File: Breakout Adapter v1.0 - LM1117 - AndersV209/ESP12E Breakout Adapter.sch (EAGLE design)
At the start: 11 parts, among them IC1 LM1117-3.3

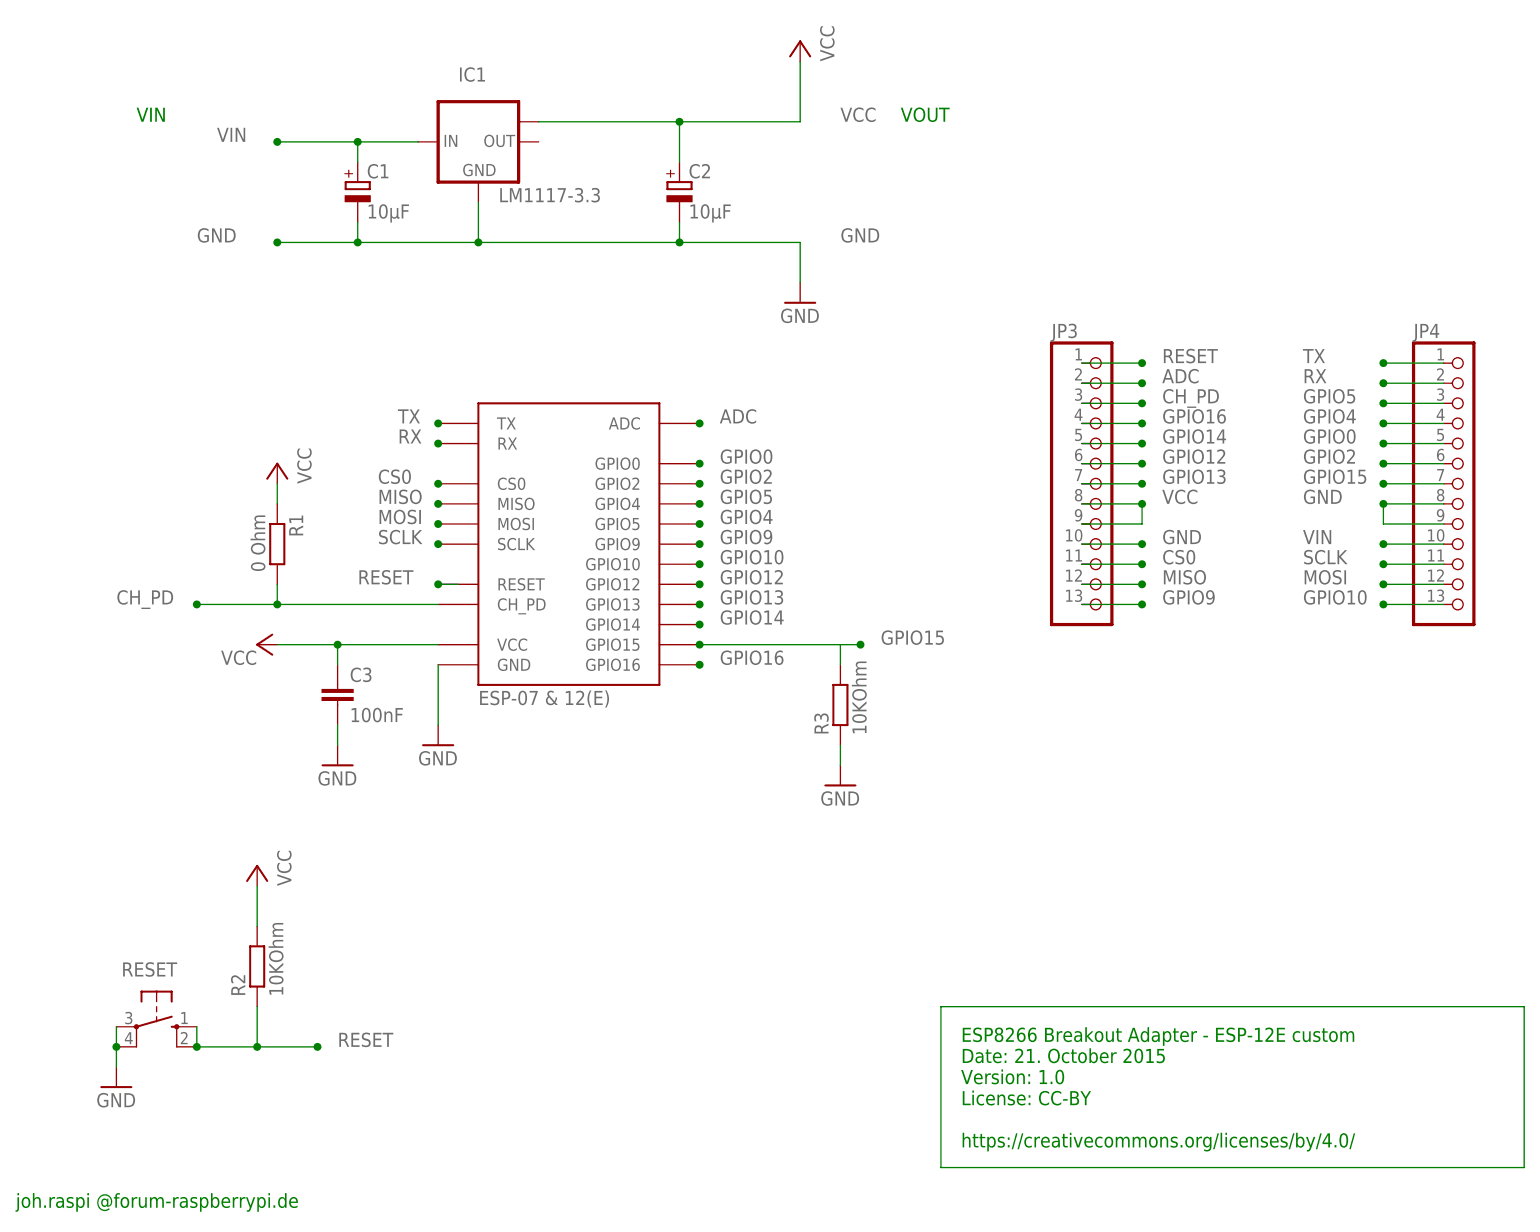
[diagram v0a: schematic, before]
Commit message: esp moved and right capacitor footprint chosen
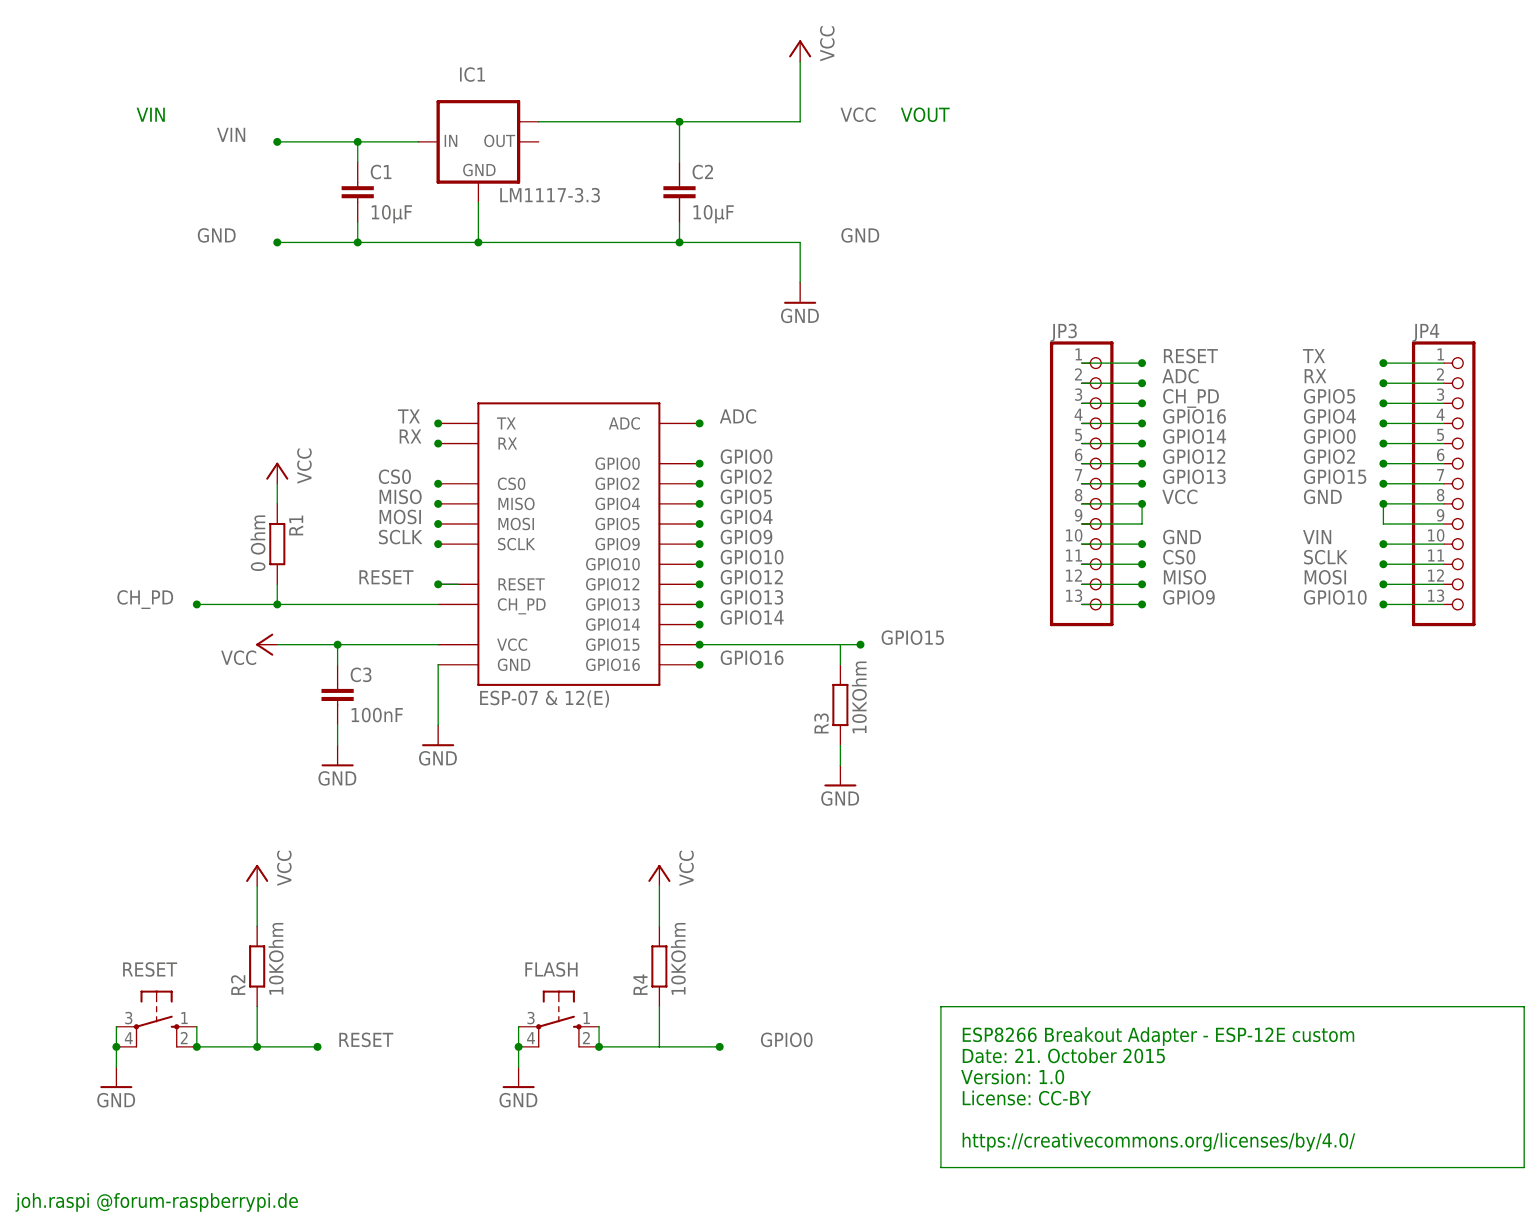
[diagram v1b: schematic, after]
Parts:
- added FLASH_SWITCH: FLASH, switch-omron:10-XX
- added R4: 10KOhm, rcl:R-EU_R0805
- C1, C2: device rcl:CPOL-EUB/3528-21W -> rcl:C-EUC0805K
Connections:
- net GND: now also C1.2, C2.2, FLASH_SWITCH.P, FLASH_SWITCH.P1; no longer C1.-, C2.-
- net GPIO0: now also FLASH_SWITCH.S, FLASH_SWITCH.S1, R4.1
- net VCC: now also C2.1, R4.2; no longer C2.+
- net VIN: now also C1.1; no longer C1.+
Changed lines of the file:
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@@
 <part name="JP4" library="pinhead" deviceset="PINHD-1X13" device=""/>
 <part name="IC1" library="lm1117" deviceset="LM1117MPX-*" device="" technology="3.3" value="LM1117-3.3"/>
-<part name="C1" library="rcl" deviceset="CPOL-EU" device="B/3528-21W" value="10µF"/>
+<part name="C1" library="rcl" deviceset="C-EU" device="C0805K" value="10µF"/>
 <part name="C3" library="rcl" deviceset="C-EU" device="C0805K" value="100nF"/>
-<part name="C2" library="rcl" deviceset="CPOL-EU" device="B/3528-21W" value="10µF"/>
+<part name="C2" library="rcl" deviceset="C-EU" device="C0805K" value="10µF"/>
 <part name="R1" library="rcl" deviceset="R-EU_" device="R0805" value="0 Ohm"/>
 <part name="RESET_SWITCH" library="switch-omron" deviceset="10-XX" device="" value="RESET"/>
@@
 <part name="R3" library="rcl" deviceset="R-EU_" device="R0805" value="10KOhm"/>
 <part name="GND2" library="supply1" deviceset="GND" device=""/>
+<part name="FLASH_SWITCH" library="switch-omron" deviceset="10-XX" device="" value="FLASH"/>
+<part name="GND5" library="supply1" deviceset="GND" device=""/>
+<part name="R4" library="rcl" deviceset="R-EU_" device="R0805" value="10KOhm"/>
+<part name="3V3" library="supply1" deviceset="VCC" device=""/>
 </parts>
 <sheets>
@@
 <instance part="R3" gate="G$1" x="129.54" y="58.42" rot="R90"/>
 <instance part="GND2" gate="1" x="129.54" y="48.26"/>
+<instance part="FLASH_SWITCH" gate="1" x="93.98" y="17.78" smashed="yes" rot="R270">
+<attribute name="VALUE" x="89.535" y="24.13" size="1.778" layer="96"/>
+</instance>
+<instance part="GND5" gate="1" x="88.9" y="10.16"/>
+<instance part="R4" gate="G$1" x="106.68" y="25.4" rot="R90"/>
+<instance part="3V3" gate="VCC" x="106.68" y="38.1" rot="MR0"/>
 </instances>
 <busses>
@@
 <net name="GND" class="1">
 <segment>
-<pinref part="C1" gate="G$1" pin="-"/>
+<pinref part="C1" gate="G$1" pin="2"/>
 <wire x1="58.42" y1="116.84" x2="68.58" y2="116.84" width="0.1524" layer="91"/>
 <pinref part="IC1" gate="G$1" pin="GND"/>
 <wire x1="68.58" y1="119.38" x2="68.58" y2="116.84" width="0.1524" layer="91"/>
 <wire x1="68.58" y1="116.84" x2="83.82" y2="116.84" width="0.1524" layer="91"/>
-<pinref part="C2" gate="G$1" pin="-"/>
+<pinref part="C2" gate="G$1" pin="2"/>
 <wire x1="83.82" y1="121.92" x2="83.82" y2="116.84" width="0.1524" layer="91"/>
 <wire x1="83.82" y1="116.84" x2="109.22" y2="116.84" width="0.1524" layer="91"/>
@@
 <wire x1="129.54" y1="50.8" x2="129.54" y2="53.34" width="0.1524" layer="91"/>
 </segment>
+<segment>
+<pinref part="GND5" gate="1" pin="GND"/>
+<pinref part="FLASH_SWITCH" gate="1" pin="P1"/>
+<wire x1="88.9" y1="12.7" x2="88.9" y2="15.24" width="0.1524" layer="91"/>
+<pinref part="FLASH_SWITCH" gate="1" pin="P"/>
+<wire x1="88.9" y1="17.78" x2="88.9" y2="15.24" width="0.1524" layer="91"/>
+<junction x="88.9" y="15.24"/>
+</segment>
 </net>
 <net name="VCC" class="0">
 <segment>
-<pinref part="C2" gate="G$1" pin="+"/>
+<pinref part="C2" gate="G$1" pin="1"/>
 <wire x1="124.46" y1="132.08" x2="109.22" y2="132.08" width="0.1524" layer="91"/>
 <pinref part="IC1" gate="G$1" pin="OUT1"/>
@@
 <wire x1="167.64" y1="81.28" x2="167.64" y2="83.82" width="0.1524" layer="91"/>
 </segment>
+<segment>
+<pinref part="R4" gate="G$1" pin="2"/>
+<pinref part="3V3" gate="VCC" pin="VCC"/>
+<wire x1="106.68" y1="30.48" x2="106.68" y2="35.56" width="0.1524" layer="91"/>
+</segment>
 </net>
 <net name="GPIO0" class="0">
@@
 <junction x="198.12" y="91.44"/>
 <label x="187.96" y="91.44" size="1.778" layer="95"/>
+</segment>
+<segment>
+<pinref part="R4" gate="G$1" pin="1"/>
+<wire x1="106.68" y1="20.32" x2="106.68" y2="15.24" width="0.1524" layer="91"/>
+<pinref part="FLASH_SWITCH" gate="1" pin="S1"/>
+<wire x1="106.68" y1="15.24" x2="99.06" y2="15.24" width="0.1524" layer="91"/>
+<pinref part="FLASH_SWITCH" gate="1" pin="S"/>
+<wire x1="99.06" y1="15.24" x2="99.06" y2="17.78" width="0.1524" layer="91"/>
+<wire x1="106.68" y1="15.24" x2="114.3" y2="15.24" width="0.1524" layer="91"/>
+<junction x="99.06" y="15.24"/>
+<junction x="114.3" y="15.24"/>
+<label x="119.38" y="15.24" size="1.778" layer="95"/>
 </segment>
 </net>
@@
 <net name="VIN" class="0">
 <segment>
-<pinref part="C1" gate="G$1" pin="+"/>
+<pinref part="C1" gate="G$1" pin="1"/>
 <wire x1="58.42" y1="129.54" x2="68.58" y2="129.54" width="0.1524" layer="91"/>
 <wire x1="68.58" y1="129.54" x2="68.58" y2="127" width="0.1524" layer="91"/>
